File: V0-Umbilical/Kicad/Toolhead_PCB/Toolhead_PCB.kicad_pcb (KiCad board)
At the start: 2 copper layers, 49.8 x 28 mm, 10 parts, among them J1 Conn_02x07_Top_Bottom, J2 Motor, J3 Hotend Fan, J4 Part Cooling Fan, J5 Heater, J6 Thermistor, J7 X-Endstop, J8 Part Cooling Fan

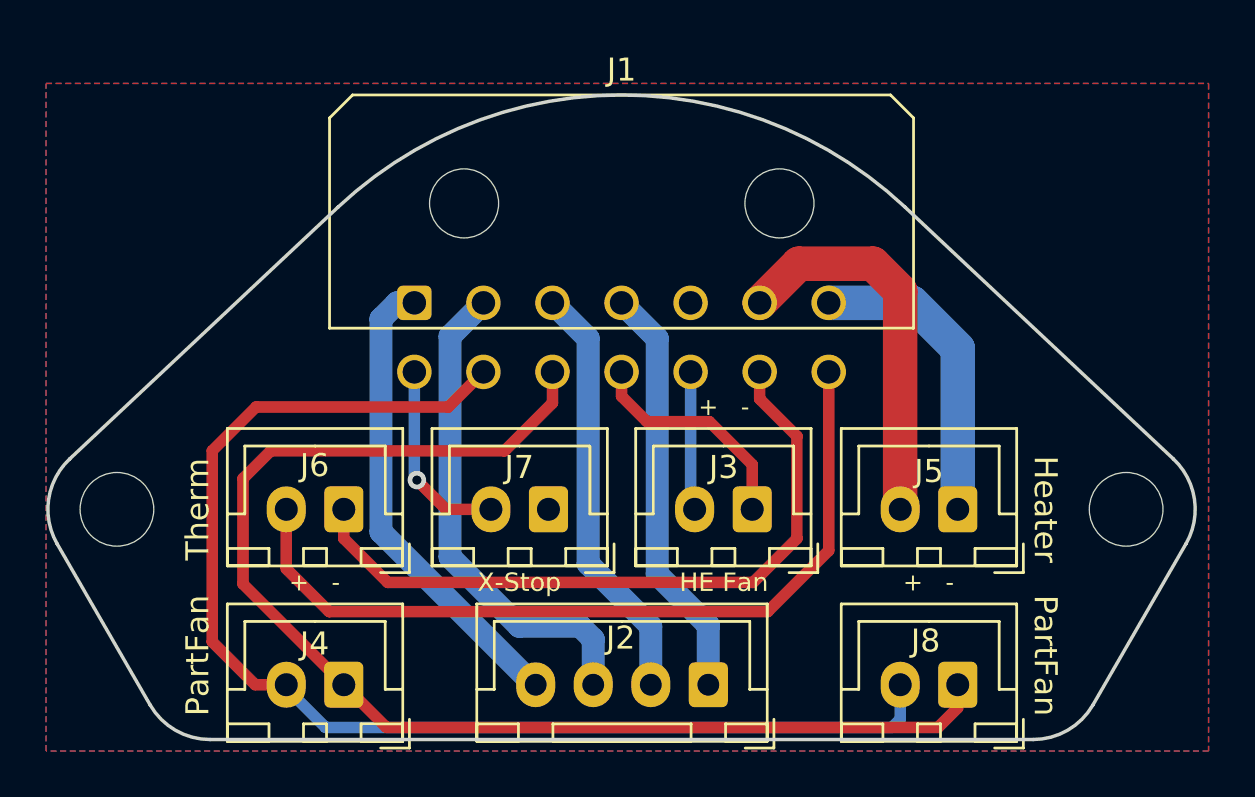
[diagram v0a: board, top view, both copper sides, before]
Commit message: First attempt at adding a SuperPINDA connector.
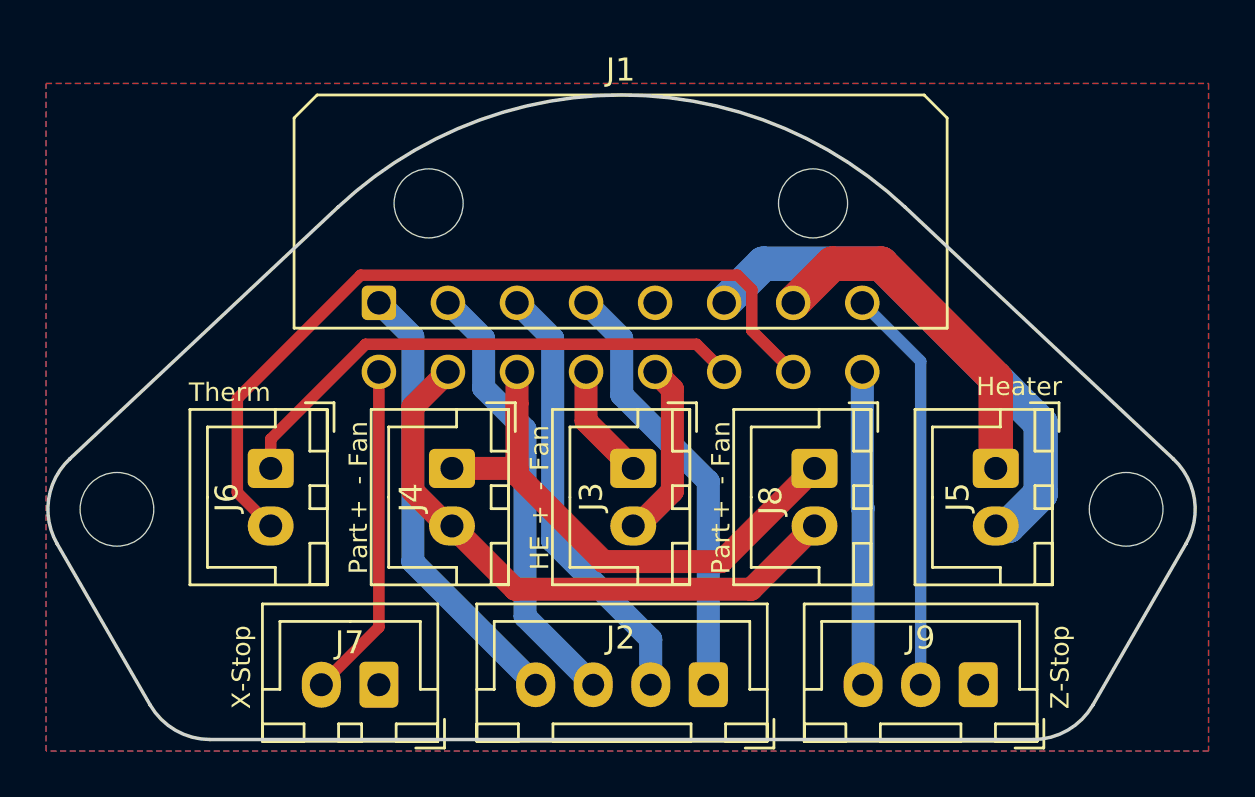
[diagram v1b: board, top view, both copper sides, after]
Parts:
- added J9: SuperPINDA, Connector_JST:JST_XH_B3B-XH-A_1x03_P2.50mm_Vertical, F.Cu at (115.5, 107.6)
- J1: value Conn_02x07_Top_Bottom -> Conn_02x08Top_Bottom; footprint Toolhead_PCB:Molex_Micro-Fit_3.0_43045-1400_2x07_P3.00mm_Horizontal -> Connector_Molex:Molex_Micro-Fit_3.0_43045-1600_2x08_P3.00mm_Horizontal
- moved J8 11.3 mm to (108.4, 98.2), turned to 270 degrees
- moved J7 10.6 mm to (89.5, 107.6)
- moved J4 10.5 mm to (92.6, 98.2), turned to 270 degrees
- moved J3 5.46 mm to (100.5, 98.2), turned to 270 degrees
- moved J6 3.64 mm to (84.8, 98.2), turned to 270 degrees
- moved J5 2.43 mm to (116.3, 98.2), turned to 270 degrees
- moved J1 1.54 mm to (89.5, 91.0)
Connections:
- J1 pad 10: /PartFan- -> /PartFan+
- J1 pad 11: /Hotend_Fan- -> /PartFan-
- J1 pad 12: /Hotend_Fan+ -> /Hotend_Fan-
- J1 pad 13: /Thermistor_1 -> /Hotend_Fan+
- J1 pad 14: /Thermistor_2 -> /Thermistor_1
- J1 pad 8: /Endstop_Sig -> /Z-Endstop
- J1 pad 9: /PartFan+ -> /Endstop_Sig
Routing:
- net /PartFan-: track 55.7 -> 23.5 mm
- net /PartFan+: track 54.7 -> 26.2 mm
- net /Z-Endstop: track 0.00 -> 17.6 mm
- net /5V: track 0.00 -> 13.6 mm
- net /Thermistor_1: track 30.4 -> 23.2 mm
- net /Endstop_Sig: track 8.49 -> 14.6 mm, vias 1 -> 0
- net /Heater2: track 16.8 -> 22.9 mm
- net /Hotend_Fan-: track 9.91 -> 5.04 mm
- net /Motor_A2: track 21.3 -> 19.2 mm
- net /Heater1: track 13.4 -> 15.5 mm
- net /Hotend_Fan+: track 6.04 -> 7.82 mm
- net /Motor_A1: track 20.5 -> 19.5 mm
- net /Motor_B2: track 18.2 -> 18.8 mm
- net /Motor_B1: track 18.4 -> 19.0 mm
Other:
- board text added: "Part Fan"
- board text added: "Z-Stop"
- board text removed: "PartFan"
